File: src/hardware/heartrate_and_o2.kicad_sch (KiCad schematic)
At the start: 5 parts, among them U16 MAX30101EFD_T

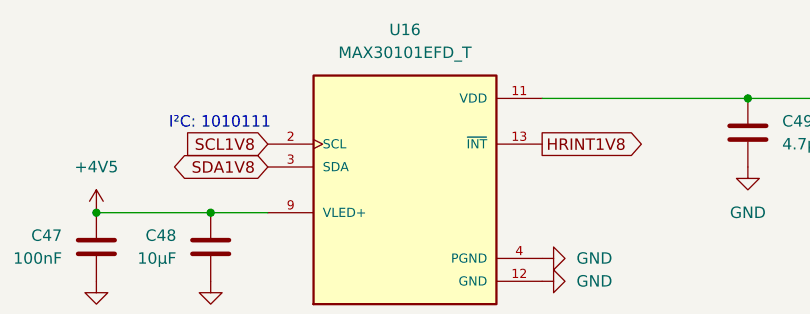
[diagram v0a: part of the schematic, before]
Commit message: Add Light Sensor and Proximity & Gesture Sensor; Changed GPIO
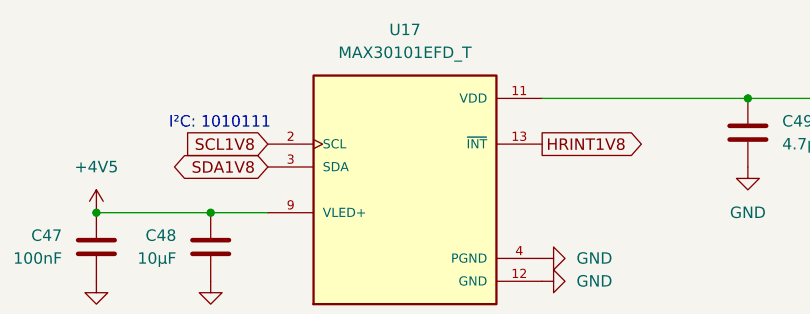
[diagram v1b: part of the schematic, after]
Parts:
- renumbered U16 to U17
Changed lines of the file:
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@@
 		(dnp no)
 		(fields_autoplaced yes)
-		(property "Reference" "#PWR0303"
+		(property "Reference" "#PWR0307"
 			(at 198.12 90.17 0)
 			(effects
@@
 			(project "raywatch"
 				(path "/7b654ee8-2a53-4d39-8b7d-32c7bb3cb0ed/92973ecd-838d-4692-844f-05a1efeb365a"
-					(reference "#PWR0303")
+					(reference "#PWR0307")
 					(unit 1)
 				)
@@
 		(dnp no)
 		(fields_autoplaced yes)
-		(property "Reference" "#PWR0299"
+		(property "Reference" "#PWR0303"
 			(at 125.73 113.03 0)
 			(effects
@@
 			(project "raywatch"
 				(path "/7b654ee8-2a53-4d39-8b7d-32c7bb3cb0ed/92973ecd-838d-4692-844f-05a1efeb365a"
-					(reference "#PWR0299")
+					(reference "#PWR0303")
 					(unit 1)
 				)
@@
 		(dnp no)
 		(fields_autoplaced yes)
-		(property "Reference" "#PWR0302"
+		(property "Reference" "#PWR0306"
 			(at 185.42 100.33 0)
 			(effects
@@
 			(project "raywatch"
 				(path "/7b654ee8-2a53-4d39-8b7d-32c7bb3cb0ed/92973ecd-838d-4692-844f-05a1efeb365a"
-					(reference "#PWR0302")
+					(reference "#PWR0306")
 					(unit 1)
 				)
@@
 		(dnp no)
 		(fields_autoplaced yes)
-		(property "Reference" "#PWR0297"
+		(property "Reference" "#PWR0301"
 			(at 113.03 102.87 0)
 			(effects
@@
 			(project "raywatch"
 				(path "/7b654ee8-2a53-4d39-8b7d-32c7bb3cb0ed/92973ecd-838d-4692-844f-05a1efeb365a"
-					(reference "#PWR0297")
+					(reference "#PWR0301")
 					(unit 1)
 				)
@@
 		(dnp no)
 		(fields_autoplaced yes)
-		(property "Reference" "#PWR0300"
+		(property "Reference" "#PWR0304"
 			(at 168.91 104.14 0)
 			(effects
@@
 			(project "raywatch"
 				(path "/7b654ee8-2a53-4d39-8b7d-32c7bb3cb0ed/92973ecd-838d-4692-844f-05a1efeb365a"
-					(reference "#PWR0300")
+					(reference "#PWR0304")
 					(unit 1)
 				)
@@
 		(dnp no)
 		(fields_autoplaced yes)
-		(property "Reference" "U16"
+		(property "Reference" "U17"
 			(at 147.32 78.74 0)
 			(effects
@@
 			(project "raywatch"
 				(path "/7b654ee8-2a53-4d39-8b7d-32c7bb3cb0ed/92973ecd-838d-4692-844f-05a1efeb365a"
-					(reference "U16")
+					(reference "U17")
 					(unit 1)
 				)
@@
 		(dnp no)
 		(fields_autoplaced yes)
-		(property "Reference" "#PWR0304"
+		(property "Reference" "#PWR0308"
 			(at 198.12 100.33 0)
 			(effects
@@
 			(project "raywatch"
 				(path "/7b654ee8-2a53-4d39-8b7d-32c7bb3cb0ed/92973ecd-838d-4692-844f-05a1efeb365a"
-					(reference "#PWR0304")
+					(reference "#PWR0308")
 					(unit 1)
 				)
@@
 		(dnp no)
 		(fields_autoplaced yes)
-		(property "Reference" "#PWR0301"
+		(property "Reference" "#PWR0305"
 			(at 168.91 106.68 0)
 			(effects
@@
 			(project "raywatch"
 				(path "/7b654ee8-2a53-4d39-8b7d-32c7bb3cb0ed/92973ecd-838d-4692-844f-05a1efeb365a"
-					(reference "#PWR0301")
+					(reference "#PWR0305")
 					(unit 1)
 				)
@@
 		(dnp no)
 		(fields_autoplaced yes)
-		(property "Reference" "#PWR0298"
+		(property "Reference" "#PWR0302"
 			(at 113.03 113.03 0)
 			(effects
@@
 			(project "raywatch"
 				(path "/7b654ee8-2a53-4d39-8b7d-32c7bb3cb0ed/92973ecd-838d-4692-844f-05a1efeb365a"
-					(reference "#PWR0298")
-					(unit 1)
-				)
+					(reference "#PWR0302")
+					(unit 1)
+				)

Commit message: Changed footprints from 0603 to 0402
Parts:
- C47, C48, C49, C50: footprint Capacitor_SMD:C_0603_1608Metric -> Capacitor_SMD:C_0504_1310Metric
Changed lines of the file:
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@@
 			)
 		)
-		(property "Footprint" "Capacitor_SMD:C_0603_1608Metric"
+		(property "Footprint" "Capacitor_SMD:C_0504_1310Metric"
 			(at 112.0648 106.68 0)
 			(effects
@@
 			)
 		)
-		(property "Footprint" "Capacitor_SMD:C_0603_1608Metric"
+		(property "Footprint" "Capacitor_SMD:C_0504_1310Metric"
 			(at 197.1548 93.98 0)
 			(effects
@@
 			)
 		)
-		(property "Footprint" "Capacitor_SMD:C_0603_1608Metric"
+		(property "Footprint" "Capacitor_SMD:C_0504_1310Metric"
 			(at 124.7648 106.68 0)
 			(effects
@@
 			)
 		)
-		(property "Footprint" "Capacitor_SMD:C_0603_1608Metric"
+		(property "Footprint" "Capacitor_SMD:C_0504_1310Metric"
 			(at 184.4548 93.98 0)
 			(effects

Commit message: Replaced global labels with pin headers
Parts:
- added J30: Conn_01x01_Pin, symbol Connector:Conn_01x01_Pin
- added J45, J46, J48: Conn_01x02_Pin, symbol Connector:Conn_01x02_Pin
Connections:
- net +1V8: now also J46.1 (Pin_1)
- net +4V5: now also J45.1 (Pin_1)
- net GND: now also J45.2 (Pin_2), J46.2 (Pin_2)
- net HRINT1V8: now also J30.1 (Pin_1)
- net SCL1V8: now also J48.1 (Pin_1)
- net SDA1V8: now also J48.2 (Pin_2)

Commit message: Reannotated schematic
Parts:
- renumbered C47 to C41, C48 to C42, C49 to C43, C50 to C44, J45 to J52, J46 to J53, J30 to J54, J48 to J55
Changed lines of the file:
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@@
 		(dnp no)
 		(fields_autoplaced yes)
-		(property "Reference" "C47"
+		(property "Reference" "C41"
 			(at 109.22 101.5999 0)
 			(effects
@@
 			(project "raywatch"
 				(path "/7b654ee8-2a53-4d39-8b7d-32c7bb3cb0ed/92973ecd-838d-4692-844f-05a1efeb365a"
-					(reference "C47")
+					(reference "C41")
 					(unit 1)
 				)
@@
 		(dnp no)
 		(fields_autoplaced yes)
-		(property "Reference" "J48"
+		(property "Reference" "J55"
 			(at 123.825 77.47 0)
 			(effects
@@
 			(project "raywatch"
 				(path "/7b654ee8-2a53-4d39-8b7d-32c7bb3cb0ed/92973ecd-838d-4692-844f-05a1efeb365a"
-					(reference "J48")
+					(reference "J55")
 					(unit 1)
 				)
@@
 		(dnp no)
 		(fields_autoplaced yes)
-		(property "Reference" "#PWR0482"
+		(property "Reference" "#PWR0310"
 			(at 134.62 55.88 0)
 			(effects
@@
 			(project "raywatch"
 				(path "/7b654ee8-2a53-4d39-8b7d-32c7bb3cb0ed/92973ecd-838d-4692-844f-05a1efeb365a"
-					(reference "#PWR0482")
+					(reference "#PWR0310")
 					(unit 1)
 				)
@@
 		(dnp no)
 		(fields_autoplaced yes)
-		(property "Reference" "#PWR0307"
+		(property "Reference" "#PWR0316"
 			(at 198.12 90.17 0)
 			(effects
@@
 			(project "raywatch"
 				(path "/7b654ee8-2a53-4d39-8b7d-32c7bb3cb0ed/92973ecd-838d-4692-844f-05a1efeb365a"
-					(reference "#PWR0307")
+					(reference "#PWR0316")
 					(unit 1)
 				)
@@
 		(dnp no)
 		(fields_autoplaced yes)
-		(property "Reference" "J46"
+		(property "Reference" "J53"
 			(at 123.825 58.42 0)
 			(effects
@@
 			(project "raywatch"
 				(path "/7b654ee8-2a53-4d39-8b7d-32c7bb3cb0ed/92973ecd-838d-4692-844f-05a1efeb365a"
-					(reference "J46")
+					(reference "J53")
 					(unit 1)
 				)
@@
 		(dnp no)
 		(fields_autoplaced yes)
-		(property "Reference" "#PWR0303"
+		(property "Reference" "#PWR0308"
 			(at 125.73 113.03 0)
 			(effects
@@
 			(project "raywatch"
 				(path "/7b654ee8-2a53-4d39-8b7d-32c7bb3cb0ed/92973ecd-838d-4692-844f-05a1efeb365a"
-					(reference "#PWR0303")
+					(reference "#PWR0308")
 					(unit 1)
 				)
@@
 		(dnp no)
 		(fields_autoplaced yes)
-		(property "Reference" "#PWR0484"
+		(property "Reference" "#PWR0309"
 			(at 124.46 53.34 0)
 			(effects
@@
 			(project "raywatch"
 				(path "/7b654ee8-2a53-4d39-8b7d-32c7bb3cb0ed/92973ecd-838d-4692-844f-05a1efeb365a"
-					(reference "#PWR0484")
+					(reference "#PWR0309")
 					(unit 1)
 				)
@@
 		(dnp no)
 		(fields_autoplaced yes)
-		(property "Reference" "#PWR0306"
+		(property "Reference" "#PWR0315"
 			(at 185.42 100.33 0)
 			(effects
@@
 			(project "raywatch"
 				(path "/7b654ee8-2a53-4d39-8b7d-32c7bb3cb0ed/92973ecd-838d-4692-844f-05a1efeb365a"
-					(reference "#PWR0306")
+					(reference "#PWR0315")
 					(unit 1)
 				)
@@
 		(dnp no)
 		(fields_autoplaced yes)
-		(property "Reference" "J30"
+		(property "Reference" "J54"
 			(at 123.825 68.58 0)
 			(effects
@@
 			(project "raywatch"
 				(path "/7b654ee8-2a53-4d39-8b7d-32c7bb3cb0ed/92973ecd-838d-4692-844f-05a1efeb365a"
-					(reference "J30")
+					(reference "J54")
 					(unit 1)
 				)
@@
 		(dnp no)
 		(fields_autoplaced yes)
-		(property "Reference" "#PWR0301"
+		(property "Reference" "#PWR0306"
 			(at 113.03 102.87 0)
 			(effects
@@
 			(project "raywatch"
 				(path "/7b654ee8-2a53-4d39-8b7d-32c7bb3cb0ed/92973ecd-838d-4692-844f-05a1efeb365a"
-					(reference "#PWR0301")
+					(reference "#PWR0306")
 					(unit 1)
 				)
@@
 		(dnp no)
 		(fields_autoplaced yes)
-		(property "Reference" "#PWR0481"
+		(property "Reference" "#PWR0312"
 			(at 134.62 66.04 0)
 			(effects
@@
 			(project "raywatch"
 				(path "/7b654ee8-2a53-4d39-8b7d-32c7bb3cb0ed/92973ecd-838d-4692-844f-05a1efeb365a"
-					(reference "#PWR0481")
+					(reference "#PWR0312")
 					(unit 1)
 				)
@@
 		(dnp no)
 		(fields_autoplaced yes)
-		(property "Reference" "C50"
+		(property "Reference" "C44"
 			(at 201.93 88.8999 0)
 			(effects
@@
 			(project "raywatch"
 				(path "/7b654ee8-2a53-4d39-8b7d-32c7bb3cb0ed/92973ecd-838d-4692-844f-05a1efeb365a"
-					(reference "C50")
+					(reference "C44")
 					(unit 1)
 				)
@@
 		(dnp no)
 		(fields_autoplaced yes)
-		(property "Reference" "#PWR0483"
+		(property "Reference" "#PWR0311"
 			(at 124.46 63.5 0)
 			(effects
@@
 			(project "raywatch"
 				(path "/7b654ee8-2a53-4d39-8b7d-32c7bb3cb0ed/92973ecd-838d-4692-844f-05a1efeb365a"
-					(reference "#PWR0483")
+					(reference "#PWR0311")
 					(unit 1)
 				)
@@
 		(dnp no)
 		(fields_autoplaced yes)
-		(property "Reference" "C48"
+		(property "Reference" "C42"
 			(at 121.92 101.5999 0)
 			(effects
@@
 			(project "raywatch"
 				(path "/7b654ee8-2a53-4d39-8b7d-32c7bb3cb0ed/92973ecd-838d-4692-844f-05a1efeb365a"
-					(reference "C48")
+					(reference "C42")
 					(unit 1)
 				)
@@
 		(dnp no)
 		(fields_autoplaced yes)
-		(property "Reference" "#PWR0304"
+		(property "Reference" "#PWR0313"
 			(at 168.91 104.14 0)
 			(effects
@@
 			(project "raywatch"
 				(path "/7b654ee8-2a53-4d39-8b7d-32c7bb3cb0ed/92973ecd-838d-4692-844f-05a1efeb365a"
-					(reference "#PWR0304")
+					(reference "#PWR0313")
 					(unit 1)
 				)
@@
 		(dnp no)
 		(fields_autoplaced yes)
-		(property "Reference" "#PWR0308"
+		(property "Reference" "#PWR0317"
 			(at 198.12 100.33 0)
 			(effects
@@
 			(project "raywatch"
 				(path "/7b654ee8-2a53-4d39-8b7d-32c7bb3cb0ed/92973ecd-838d-4692-844f-05a1efeb365a"
-					(reference "#PWR0308")
+					(reference "#PWR0317")
 					(unit 1)
 				)
@@
 		(dnp no)
 		(fields_autoplaced yes)
-		(property "Reference" "C49"
+		(property "Reference" "C43"
 			(at 189.23 88.8999 0)
 			(effects
@@
 			(project "raywatch"
 				(path "/7b654ee8-2a53-4d39-8b7d-32c7bb3cb0ed/92973ecd-838d-4692-844f-05a1efeb365a"
-					(reference "C49")
+					(reference "C43")
 					(unit 1)
 				)
@@
 		(dnp no)
 		(fields_autoplaced yes)
-		(property "Reference" "J45"
+		(property "Reference" "J52"
 			(at 123.825 48.26 0)
 			(effects
@@
 			(project "raywatch"
 				(path "/7b654ee8-2a53-4d39-8b7d-32c7bb3cb0ed/92973ecd-838d-4692-844f-05a1efeb365a"
-					(reference "J45")
+					(reference "J52")
 					(unit 1)
 				)
@@
 		(dnp no)
 		(fields_autoplaced yes)
-		(property "Reference" "#PWR0305"
+		(property "Reference" "#PWR0314"
 			(at 168.91 106.68 0)
 			(effects
@@
 			(project "raywatch"
 				(path "/7b654ee8-2a53-4d39-8b7d-32c7bb3cb0ed/92973ecd-838d-4692-844f-05a1efeb365a"
-					(reference "#PWR0305")
+					(reference "#PWR0314")
 					(unit 1)
 				)
@@
 		(dnp no)
 		(fields_autoplaced yes)
-		(property "Reference" "#PWR0302"
+		(property "Reference" "#PWR0307"
 			(at 113.03 113.03 0)
 			(effects
@@
 			(project "raywatch"
 				(path "/7b654ee8-2a53-4d39-8b7d-32c7bb3cb0ed/92973ecd-838d-4692-844f-05a1efeb365a"
-					(reference "#PWR0302")
-					(unit 1)
-				)
+					(reference "#PWR0307")
+					(unit 1)
+				)

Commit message: Assigned pin header footprints
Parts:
- J52, J53, J55: footprint (none) -> Connector_PinHeader_2.54mm:PinHeader_1x02_P2.54mm_Horizontal
- J54: footprint (none) -> Connector_PinHeader_2.54mm:PinHeader_1x01_P2.54mm_Horizontal
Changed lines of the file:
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@@
 			)
 		)
-		(property "Footprint" ""
+		(property "Footprint" "Connector_PinHeader_2.54mm:PinHeader_1x02_P2.54mm_Horizontal"
 			(at 123.19 82.55 0)
 			(effects
@@
 			)
 		)
-		(property "Footprint" ""
+		(property "Footprint" "Connector_PinHeader_2.54mm:PinHeader_1x02_P2.54mm_Horizontal"
 			(at 123.19 63.5 0)
 			(effects
@@
 			)
 		)
-		(property "Footprint" ""
+		(property "Footprint" "Connector_PinHeader_2.54mm:PinHeader_1x01_P2.54mm_Horizontal"
 			(at 123.19 73.66 0)
 			(effects
@@
 			)
 		)
-		(property "Footprint" ""
+		(property "Footprint" "Connector_PinHeader_2.54mm:PinHeader_1x02_P2.54mm_Horizontal"
 			(at 123.19 53.34 0)
 			(effects
